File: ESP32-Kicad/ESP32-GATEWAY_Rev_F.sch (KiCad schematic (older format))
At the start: 90 parts, among them CON1 NA(NH1x20), Q3 Q12MHz/20pF/30ppm/2P/HC-49SM(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, Q4 BC817-40(SOT23), Q5 BC817-40(SOT23), T1 DTC114YKA, U2 SY8089AAAC(SOT23-5), U3 ESP32-WROOM-32D-4MB, U4 LAN8710A-EZC(QFN32), U5 CH340T(SSOP20W)

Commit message: Proyecto de kicad actualizado.
 Se eliminó completamente la sección de la MicroSD
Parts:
- removed BUT1: T1107A(6x3,8x2,5MM), OLIMEX_Buttons-FP:T1107A(6x3,8x2,5MM), symbol ESP32-GATEWAY_Rev_F:SIDE_WTCM-TR(3x4)
- removed C10: 47uF/6.3V/20%/X5R/C0805, OLIMEX_RLC-FP:C_0805_5MIL_DWS, symbol ESP32-GATEWAY_Rev_F:C
- removed L4: FB0805/600R/2A, OLIMEX_RLC-FP:L_0805_5MIL_DWS, symbol ESP32-GATEWAY_Rev_F:L
- removed MICRO_SD1: TFC-WXCP11-08-LF, OLIMEX_Connectors-FP:TFC-WXCP11-08-LF, symbol ESP32-GATEWAY_Rev_F:MICRO_SD(TFC-WXCP11-08-LF)
- removed R10, R11, R9: NA/R0603, OLIMEX_RLC-FP:R_0603_5MIL_DWS, symbol ESP32-GATEWAY_Rev_F:R
- removed R16: 220R/R0603, OLIMEX_RLC-FP:R_0603_5MIL_DWS, symbol ESP32-GATEWAY_Rev_F:R
- removed R2, R7, R8: 2.2k/R0603, OLIMEX_RLC-FP:R_0603_5MIL_DWS, symbol ESP32-GATEWAY_Rev_F:R
- removed R43: 10R/R0603, OLIMEX_RLC-FP:R_0603_5MIL_DWS, symbol ESP32-GATEWAY_Rev_F:R
- removed R45: 10k/R0603, OLIMEX_RLC-FP:R_0603_5MIL_DWS, symbol ESP32-GATEWAY_Rev_F:R
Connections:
- net labels added: GPI34
- net labels removed: GPI34\BUT1
- wire segments 428 -> 383
- no-connect marks 19 -> 31
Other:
- note added: "Debil pull-down interno. Requiere de LOW para descargar codigo. Dejar desconectado o a masa. Listo"
- note added: "Dejar la pull-up para habilitar los logs\ndurante el boot. Listo"
- note added: "Incluido en el bootstrap pero no se usa. Dejado por las dudas."
- note added: "Requiere de LOW para descargar codigo\nDejar desconectado o a masa. Listo."
- note added: "Se necesita LOW o desconectado para la flash con 3v3. Listo"
- note added: "Usar. Listo"
- note removed: "Arranca con PWM. \nTestear con ds18b20"
- note removed: "Debil pull-down interno. Requiere de LOW para descargar codigo. Dejar desconectado o a masa."
- note removed: "Debil pull-down interno. Requiere de LOW para descargar codigo. Dejar desconectado o a masa. Faltaria un pulldown."
- note removed: "Dejar la pull-up para habilitar los logs\ndurante el boot. Evitar usar\n\n"
- note removed: "Incluido en el bootstrap pero no se usa. Se puede usar tranquilamente."
- note removed: "Incluido en ll bootstrap pero no se usa.\nSe puede usar tranquilamente."
- note removed: "No Usar. Listo"
- note removed: "No está\n"
- note removed: "No usar. Se necesita LOW o desconectado para la flash con 3v3."
- note removed: "No usar. Se necesita LOW o desconectado\n para la flash con 3v3.\n\n"
- note removed: "Probado con ds18b20 y pullup interno."
- note removed: "Probado con ds18b20 y pullup interno.\n"
- note removed: "Requiere de LOW para descargar codigo\nDejar desconectado o a masa."
- note removed: "SD/MMC Card"
- note removed: "Se necesita LOW o desconectado para la flash con 3v3."
- note removed: "Se puede usar con duda."
- note removed: "Solo entrada. Sin pulldown-pullup"
- moved on the sheet: R29, R3

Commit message: Proyecto de kicad actualizado
Se retiró la parte del programador USB y otras menores asociadas a esta.
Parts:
- removed C21, C22: 27pF/50V/5%/C0G/C0603, OLIMEX_RLC-FP:C_0603_5MIL_DWS, symbol ESP32-GATEWAY_Rev_F:C
- removed C23: 22uF/6.3V/20%/X5R/C0603, OLIMEX_RLC-FP:C_0603_5MIL_DWS, symbol ESP32-GATEWAY_Rev_F:C
- removed C24: 100nF/50V/20%/Y5V/C0603, OLIMEX_RLC-FP:C_0603_5MIL_DWS, symbol ESP32-GATEWAY_Rev_F:C
- removed D1, D3: 1N5819S4/SOD123, OLIMEX_Diodes-FP:SOD-123_1C-2A_KA, symbol ESP32-GATEWAY_Rev_F:D_Schottky
- removed D4: BAT54C(SOT23-3), OLIMEX_Diodes-FP:SOT23-3, symbol ESP32-GATEWAY_Rev_F:BAT54C(SOT23-3)
- removed Q3: Q12MHz/20pF/30ppm/2P/HC-49SM(SMD), OLIMEX_Crystal-FP:Q_49U3HMS, symbol ESP32-GATEWAY_Rev_F:Crystal
- removed Q4, Q5: BC817-40(SOT23), OLIMEX_Transistors-FP:SOT23, symbol ESP32-GATEWAY_Rev_F:Q_NPN_BEC
- removed R35, R40: 10k/R0603, OLIMEX_RLC-FP:R_0603_5MIL_DWS, symbol ESP32-GATEWAY_Rev_F:R
- removed R37: 220R/R0603, OLIMEX_RLC-FP:R_0603_5MIL_DWS, symbol ESP32-GATEWAY_Rev_F:R
- removed R41, R42: 1k/R0603, OLIMEX_RLC-FP:R_0603_5MIL_DWS, symbol ESP32-GATEWAY_Rev_F:R
- removed U5: CH340T(SSOP20W), OLIMEX_IC-FP:SSOP-20W, symbol ESP32-GATEWAY_Rev_F:CH340T(SSOP20W)
- added J10: Conn_01x02_Male, Connector_PinHeader_2.54mm:PinHeader_1x02_P2.54mm_Vertical, symbol Connector:Conn_01x02_Male
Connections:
- net labels removed: D_Com
- wire segments 383 -> 324
- no-connect marks 31 -> 27
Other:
- note removed: "Auto program\n"
- note removed: "DTR RTS->EN IO0"
- note removed: "Debil pull-down interno.\nRequiere de LOW para descargar codigo\nDejar desconectado o a masa."

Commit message: Proyecto de Kicad actualizado
Fuente corregida. Programador agregado. Cambios menores.
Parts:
- removed CON1: NA(NH1x20), OLIMEX_Connectors-FP:HN1x20, symbol ESP32-GATEWAY_Rev_F:CON20
- removed D2: SMBJ6.0A(DO-214AA), OLIMEX_Diodes-FP:DO214AA_1(K)-2(A), symbol ESP32-GATEWAY_Rev_F:SMBJ6.0A
- removed D6: 1N5822/SS34/SMA, OLIMEX_Diodes-FP:SMA-KA, symbol ESP32-GATEWAY_Rev_F:D_Schottky
- removed FET2: WPM2015-3/TR, OLIMEX_Transistors-FP:SOT23, symbol ESP32-GATEWAY_Rev_F:P-MOS+DIOD
- removed J10: Conn_01x02_Male, Connector_PinHeader_2.54mm:PinHeader_1x02_P2.54mm_Vertical, symbol Connector:Conn_01x02_Male
- removed LED_E1: Closed, OLIMEX_Jumpers-FP:SJ, symbol ESP32-GATEWAY_Rev_F:SJ
- removed PWRLED1: LED/RED/0603, OLIMEX_LEDs-FP:LED_0603_KA, symbol ESP32-GATEWAY_Rev_F:LED
- removed R30: 1M/R0603, OLIMEX_RLC-FP:R_0603_5MIL_DWS, symbol ESP32-GATEWAY_Rev_F:R
- removed R4: 2.2k/R0603, OLIMEX_RLC-FP:R_0603_5MIL_DWS, symbol ESP32-GATEWAY_Rev_F:R
- removed RST1: T1107A(6x3,8x2,5MM), OLIMEX_Buttons-FP:T1107A(6x3,8x2,5MM), symbol ESP32-GATEWAY_Rev_F:SIDE_WTCM-TR(3x4)
- added CON1: Conn_01x13_Male, Connector_PinHeader_2.54mm:PinHeader_1x13_P2.54mm_Vertical, symbol Connector:Conn_01x13_Male
- added J1: Conn_01x07_Male, Connector_PinHeader_2.54mm:PinHeader_1x07_P2.54mm_Horizontal, symbol Connector:Conn_01x07_Male
- C1: value 47uF/6.3V/20%/X5R/C0805 -> 10uF/6.3V/20%/X5R/C0805/1mΩ
- C3, C4: value 47uF/6.3V/20%/X5R/C0805 -> 4.7uF/6.3V/20%/X5R/C0805/1mΩ
- L2: value 2.2uH/1.5A/DCR=72mR/20%/3.00x3.00x1.50mm/CD32(NR3015T2R2M) -> 2.2uH/1.5A/DCR=35mR/20%/3.00x3.00x1.50mm/CD32(NR3015T2R2M)
- R19: value 220k/R0603 -> 442k/1%/50mW/R0603
- R20: value 49.9k/1%/R0603 -> 100k/1%/63mw/R0603
- R54: value NA/R0603 -> 10K/R0603
- U2: value SY8089AAAC(SOT23-5) -> TLV62569DBVT(SOT23-5)
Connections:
- net labels removed: +5V_EXT, +5V_USB
- wire segments 324 -> 293
- no-connect marks 27 -> 26
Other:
- note added: "(logs)\n"
- note added: "Dejado por las dudas."
- note added: "Dejado por las dudas.\n"
- note added: "ESP-WROOM-32\n MODULO"
- note added: "Fiduciales"
- note added: "Fuente de Alimentación"
- note added: "Programador"
- note removed: "+5V_Only!!!"
- note removed: "Arranca con PWM. Probado con ds18b20 y pullup interno.\n"
- note removed: "Arranca con PWM. Testear con ds18b20"
- note removed: "Buttons"
- note removed: "Debil pull-down interno. Requiere de LOW para descargar codigo. Dejar desconectado o a masa. Listo"
- note removed: "Debil pull-up interno. \nCon 1 entra a boot normal\nCon 0, descarga codigo."
- note removed: "Dejar la pull-up para habilitar los logs durante el boot. Evitar usar\n"
- note removed: "Dejar la pull-up para habilitar los logs\ndurante el boot. Listo"
- note removed: "ESP-WROOM-32\n MODULE"
- note removed: "Fiducials"
- note removed: "Incluido en el bootstrap pero no se usa. Dejado por las dudas."
- note removed: "NO usar. Lo necesita la parte de Ethernet"
- note removed: "NO usar. Lo necesita la parte de Ethernet. Listo"
- note removed: "Power Supply"
- note removed: "Requiere de LOW para descargar codigo\nDejar desconectado o a masa. Listo."
- note removed: "Se necesita LOW o desconectado para la flash con 3v3. Listo"
- note removed: "Se puede usar."
- note removed: "Se usa para habilitar el esp32. Dejar un pin para el programador externo"
- note removed: "TX/RX para programarlo\n"
- note removed: "USB to UART"
- moved on the sheet: C1, C3, C4, FID1, FID2, FID3, GND1, L2, MH1, MH2, R19, R20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

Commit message: Proyecto de kicad actualizado.
Se agregaron los conectores adecuados y se rutearon los gpio para estos. Queda pendiente ubicarlos correctamente para evitar el solapamiento de estos. Se acomodaron algunas resistencias y se eliminaron pistas viejas innecesarias.
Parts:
- removed CON1: Conn_01x13_Male, Connector_PinHeader_2.54mm:PinHeader_1x13_P2.54mm_Vertical, symbol Connector:Conn_01x13_Male
- removed USB-UART1: MISB-SWMM-5B-LF(USB_MICRO), OLIMEX_Connectors-FP:USB-MICRO_MISB-SWMM-5B_LF, symbol ESP32-GATEWAY_Rev_F:USB-MINI
- added PUERTA1, PUERTA2: Conn_01x02_Female, Connector_Molex:Molex_KK-254_AE-6410-02A_1x02_P2.54mm_Vertical, symbol Connector:Conn_01x02_Female
- added TEMP1, TEMP2: Conn_01x03_Female, Connector_Molex:Molex_KK-254_AE-6410-03A_1x03_P2.54mm_Vertical, symbol Connector:Conn_01x03_Female
- added USB-UART2: USB_B_Micro, Connector_USB:USB_Micro-B_Amphenol_10104110_Horizontal, symbol Connector:USB_B_Micro
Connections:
- net labels added: GPIO13\TEMP1, GPIO14\TEMP2, GPIO32\PUERTA1, GPIO33\PUERTA2
- net labels removed: GPIO13\HS2_DATA3, GPIO14\HS2_CLK, GPIO32, GPIO33\LED
- wire segments 293 -> 281
- no-connect marks 26 -> 20
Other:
- note added: "Sensores"
- note removed: "Dejado por las dudas.\n"
- note removed: "Extension"
- note removed: "Usar. Listo"
- note removed: "Usar. Listo\n"

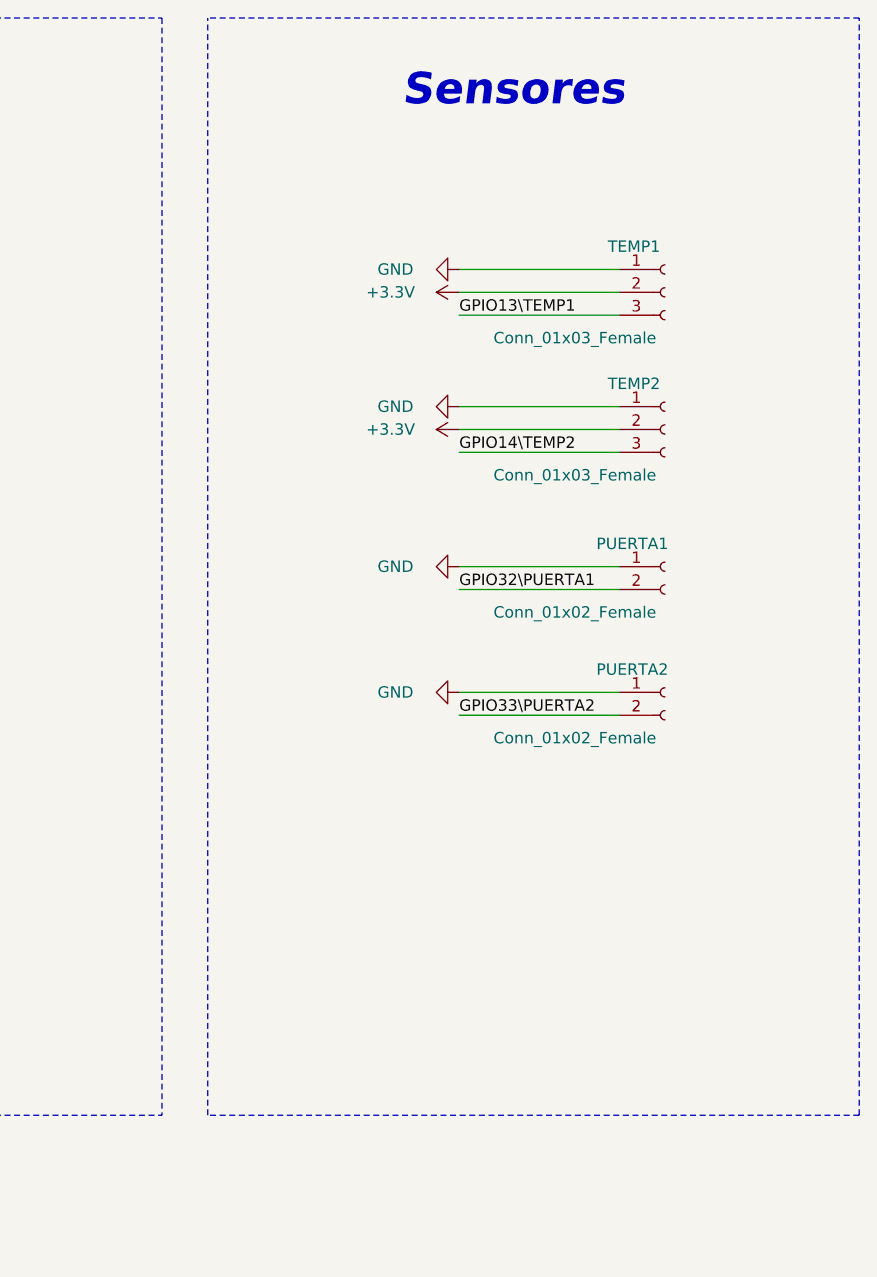
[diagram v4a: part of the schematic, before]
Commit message: Proyecto en kicad actualizado
Se modificó la posición de la pinera para programar la placa. Recolocaron los conectores de los sensores y se agregaron sus resistencias mas el modelo 3D de todo esto.
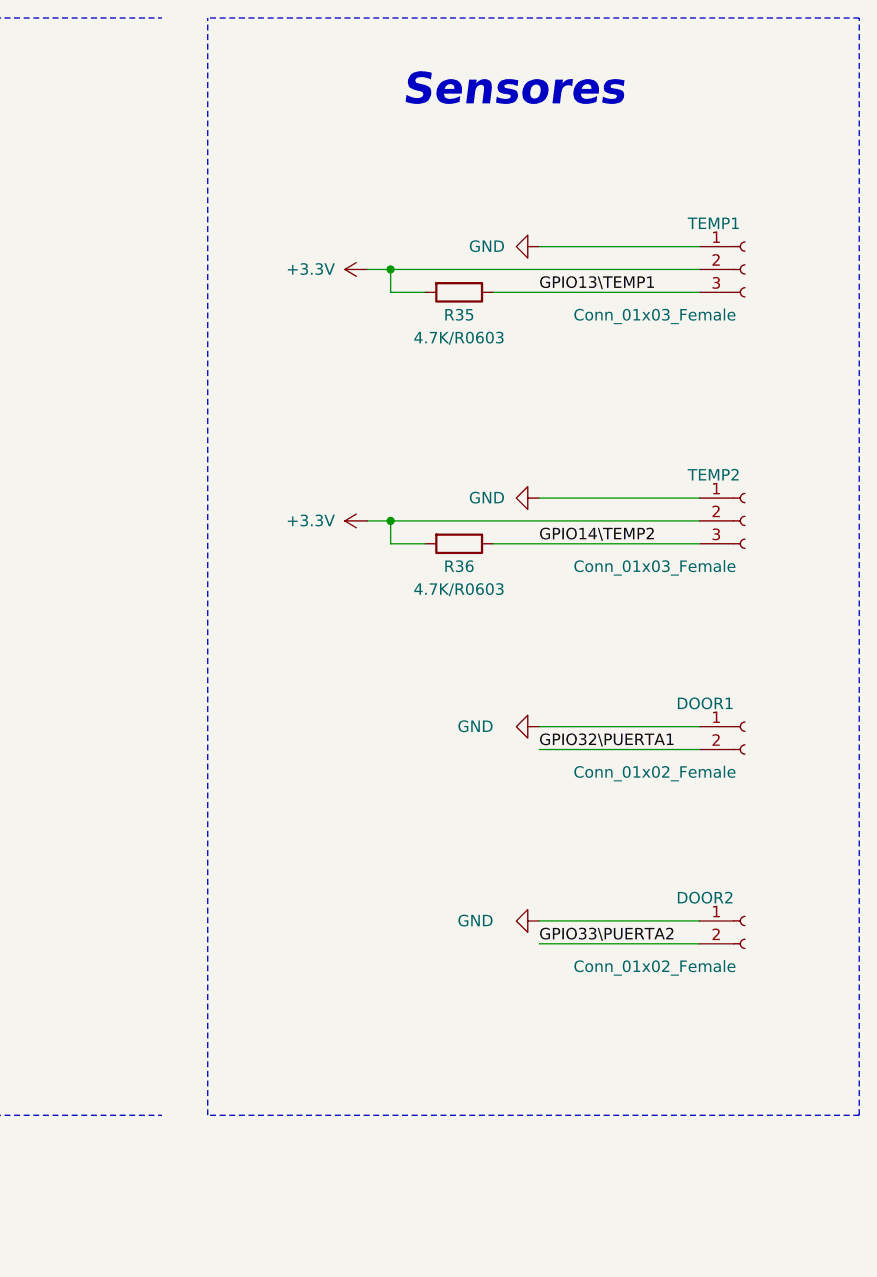
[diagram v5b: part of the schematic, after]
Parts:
- added R35, R36: 4.7K/R0603, Resistor_SMD:R_0603_1608Metric_Pad0.98x0.95mm_HandSolder, symbol Device:R
- J1: footprint Connector_PinHeader_2.54mm:PinHeader_1x07_P2.54mm_Horizontal -> Connector_PinHeader_2.54mm:PinHeader_1x07_P2.54mm_Vertical
- renumbered PUERTA1 to DOOR1, PUERTA2 to DOOR2
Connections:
- wire segments 281 -> 287
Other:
- moved on the sheet: DOOR1, DOOR2, TEMP1, TEMP2
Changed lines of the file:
@@
 F 0 "J1" H 15222 6874 50  0000 R CNN
 F 1 "Conn_01x07_Male" H 15222 6783 50  0000 R CNN
-F 2 "Connector_PinHeader_2.54mm:PinHeader_1x07_P2.54mm_Horizontal" H 15250 6850 50  0001 C CNN
+F 2 "Connector_PinHeader_2.54mm:PinHeader_1x07_P2.54mm_Vertical" H 15250 6850 50  0001 C CNN
 F 3 "~" H 15250 6850 50  0001 C CNN
 	1    15250 6850
@@
 	15050 6850 13750 6850
 Wire Notes Line
-	19550 700  19550 5500
-Wire Notes Line
 	19750 5500 19750 700
 Text Label 13750 6950 0    50   ~ 0
@@
 NoConn ~ 2000 2650
 $Comp
-L Connector:Conn_01x02_Female PUERTA1
+L Connector:Conn_01x02_Female DOOR1
 U 1 1 61288657
-P 21750 3100
-F 0 "PUERTA1" H 21450 3200 50  0000 L CNN
-F 1 "Conn_01x02_Female" H 21000 2900 50  0000 L CNN
-F 2 "Connector_Molex:Molex_KK-254_AE-6410-02A_1x02_P2.54mm_Vertical" H 21750 3100 50  0001 C CNN
-F 3 "~" H 21750 3100 50  0001 C CNN
-	1    21750 3100
-	1    0    0    -1
-$EndComp
-$Comp
-L Connector:Conn_01x02_Female PUERTA2
+P 22100 3800
+F 0 "DOOR1" H 21800 3900 50  0000 L CNN
+F 1 "Conn_01x02_Female" H 21350 3600 50  0000 L CNN
+F 2 "Connector_Molex:Molex_KK-254_AE-6410-02A_1x02_P2.54mm_Vertical" H 22100 3800 50  0001 C CNN
+F 3 "~" H 22100 3800 50  0001 C CNN
+	1    22100 3800
+	1    0    0    -1
+$EndComp
+$Comp
+L Connector:Conn_01x02_Female DOOR2
 U 1 1 6128A81D
-P 21750 3650
-F 0 "PUERTA2" H 21450 3750 50  0000 L CNN
-F 1 "Conn_01x02_Female" H 21000 3450 50  0000 L CNN
-F 2 "Connector_Molex:Molex_KK-254_AE-6410-02A_1x02_P2.54mm_Vertical" H 21750 3650 50  0001 C CNN
-F 3 "~" H 21750 3650 50  0001 C CNN
-	1    21750 3650
+P 22100 4650
+F 0 "DOOR2" H 21800 4750 50  0000 L CNN
+F 1 "Conn_01x02_Female" H 21350 4450 50  0000 L CNN
+F 2 "Connector_Molex:Molex_KK-254_AE-6410-02A_1x02_P2.54mm_Vertical" H 22100 4650 50  0001 C CNN
+F 3 "~" H 22100 4650 50  0001 C CNN
+	1    22100 4650
 	1    0    0    -1
 $EndComp
@@
 L ESP32-GATEWAY_Rev_F:GND #PWR0102
 U 1 1 6128BF60
-P 20850 3650
-F 0 "#PWR0102" H 20850 3400 50  0001 C CNN
-F 1 "GND" V 20850 3450 50  0000 R CNN
-F 2 "" H 20850 3650 60  0000 C CNN
-F 3 "" H 20850 3650 60  0000 C CNN
-	1    20850 3650
+P 21200 4650
+F 0 "#PWR0102" H 21200 4400 50  0001 C CNN
+F 1 "GND" V 21200 4450 50  0000 R CNN
+F 2 "" H 21200 4650 60  0000 C CNN
+F 3 "" H 21200 4650 60  0000 C CNN
+	1    21200 4650
 	0    1    1    0
 $EndComp
@@
 L ESP32-GATEWAY_Rev_F:GND #PWR0103
 U 1 1 612A5050
-P 20850 3100
-F 0 "#PWR0103" H 20850 2850 50  0001 C CNN
-F 1 "GND" V 20850 2900 50  0000 R CNN
-F 2 "" H 20850 3100 60  0000 C CNN
-F 3 "" H 20850 3100 60  0000 C CNN
-	1    20850 3100
-	0    1    1    0
-$EndComp
-Text Label 20850 3750 0    50   ~ 0
+P 21200 3800
+F 0 "#PWR0103" H 21200 3550 50  0001 C CNN
+F 1 "GND" V 21200 3600 50  0000 R CNN
+F 2 "" H 21200 3800 60  0000 C CNN
+F 3 "" H 21200 3800 60  0000 C CNN
+	1    21200 3800
+	0    1    1    0
+$EndComp
+Text Label 21200 4750 0    50   ~ 0
 GPIO33\PUERTA2
 $Comp
 L Connector:Conn_01x03_Female TEMP1
 U 1 1 614AF2AC
-P 21750 1900
-F 0 "TEMP1" H 21500 2100 50  0000 L CNN
-F 1 "Conn_01x03_Female" H 21000 1700 50  0000 L CNN
-F 2 "Connector_Molex:Molex_KK-254_AE-6410-03A_1x03_P2.54mm_Vertical" H 21750 1900 50  0001 C CNN
-F 3 "~" H 21750 1900 50  0001 C CNN
-	1    21750 1900
+P 22100 1800
+F 0 "TEMP1" H 21850 2000 50  0000 L CNN
+F 1 "Conn_01x03_Female" H 21350 1600 50  0000 L CNN
+F 2 "Connector_Molex:Molex_KK-254_AE-6410-03A_1x03_P2.54mm_Vertical" H 22100 1800 50  0001 C CNN
+F 3 "~" H 22100 1800 50  0001 C CNN
+	1    22100 1800
 	1    0    0    -1
 $EndComp
@@
 L Connector:Conn_01x03_Female TEMP2
 U 1 1 614B142C
-P 21750 2500
-F 0 "TEMP2" H 21500 2700 50  0000 L CNN
-F 1 "Conn_01x03_Female" H 21000 2300 50  0000 L CNN
-F 2 "Connector_Molex:Molex_KK-254_AE-6410-03A_1x03_P2.54mm_Vertical" H 21750 2500 50  0001 C CNN
-F 3 "~" H 21750 2500 50  0001 C CNN
-	1    21750 2500
+P 22100 2900
+F 0 "TEMP2" H 21850 3100 50  0000 L CNN
+F 1 "Conn_01x03_Female" H 21350 2700 50  0000 L CNN
+F 2 "Connector_Molex:Molex_KK-254_AE-6410-03A_1x03_P2.54mm_Vertical" H 22100 2900 50  0001 C CNN
+F 3 "~" H 22100 2900 50  0001 C CNN
+	1    22100 2900
 	1    0    0    -1
 $EndComp
@@
 L ESP32-GATEWAY_Rev_F:+3.3V #PWR0104
 U 1 1 614B2E1D
-P 20850 1900
-F 0 "#PWR0104" H 20850 1750 50  0001 C CNN
-F 1 "+3.3V" V 20850 2200 50  0000 C CNN
-F 2 "" H 20850 1900 60  0000 C CNN
-F 3 "" H 20850 1900 60  0000 C CNN
-	1    20850 1900
+P 20450 1800
+F 0 "#PWR0104" H 20450 1650 50  0001 C CNN
+F 1 "+3.3V" V 20450 2050 50  0000 C CNN
+F 2 "" H 20450 1800 60  0000 C CNN
+F 3 "" H 20450 1800 60  0000 C CNN
+	1    20450 1800
 	0    -1   -1   0
 $EndComp
@@
 L ESP32-GATEWAY_Rev_F:+3.3V #PWR0105
 U 1 1 614CCBB7
-P 20850 2500
-F 0 "#PWR0105" H 20850 2350 50  0001 C CNN
-F 1 "+3.3V" V 20850 2800 50  0000 C CNN
-F 2 "" H 20850 2500 60  0000 C CNN
-F 3 "" H 20850 2500 60  0000 C CNN
-	1    20850 2500
+P 20450 2900
+F 0 "#PWR0105" H 20450 2750 50  0001 C CNN
+F 1 "+3.3V" V 20450 3150 50  0000 C CNN
+F 2 "" H 20450 2900 60  0000 C CNN
+F 3 "" H 20450 2900 60  0000 C CNN
+	1    20450 2900
 	0    -1   -1   0
 $EndComp
-Text Label 20850 3200 0    50   ~ 0
+Text Label 21200 3900 0    50   ~ 0
 GPIO32\PUERTA1
 $Comp
 L ESP32-GATEWAY_Rev_F:GND #PWR0106
 U 1 1 61687BE2
-P 20850 2400
-F 0 "#PWR0106" H 20850 2150 50  0001 C CNN
-F 1 "GND" V 20850 2200 50  0000 R CNN
-F 2 "" H 20850 2400 60  0000 C CNN
-F 3 "" H 20850 2400 60  0000 C CNN
-	1    20850 2400
+P 21200 2800
+F 0 "#PWR0106" H 21200 2550 50  0001 C CNN
+F 1 "GND" V 21200 2650 50  0000 R CNN
+F 2 "" H 21200 2800 60  0000 C CNN
+F 3 "" H 21200 2800 60  0000 C CNN
+	1    21200 2800
 	0    1    1    0
 $EndComp
@@
 L ESP32-GATEWAY_Rev_F:GND #PWR0107
 U 1 1 616A2220
-P 20850 1800
-F 0 "#PWR0107" H 20850 1550 50  0001 C CNN
-F 1 "GND" V 20850 1600 50  0000 R CNN
-F 2 "" H 20850 1800 60  0000 C CNN
-F 3 "" H 20850 1800 60  0000 C CNN
-	1    20850 1800
-	0    1    1    0
-$EndComp
-Text Label 20850 2000 0    50   ~ 0
+P 21200 1700
+F 0 "#PWR0107" H 21200 1450 50  0001 C CNN
+F 1 "GND" V 21200 1550 50  0000 R CNN
+F 2 "" H 21200 1700 60  0000 C CNN
+F 3 "" H 21200 1700 60  0000 C CNN
+	1    21200 1700
+	0    1    1    0
+$EndComp
+Text Label 21200 1900 0    50   ~ 0
 GPIO13\TEMP1
-Text Label 20850 2600 0    50   ~ 0
+Text Label 21200 3000 0    50   ~ 0
 GPIO14\TEMP2
 Wire Wire Line
-	20850 2400 21550 2400
-Wire Wire Line
-	20850 2500 21550 2500
-Wire Wire Line
-	20850 2600 21550 2600
-Wire Wire Line
-	20850 1800 21550 1800
-Wire Wire Line
-	20850 1900 21550 1900
-Wire Wire Line
-	20850 2000 21550 2000
-Wire Wire Line
-	20850 3100 21550 3100
-Wire Wire Line
-	20850 3200 21550 3200
-Wire Wire Line
-	20850 3650 21550 3650
-Wire Wire Line
-	20850 3750 21550 3750
+	21200 2800 21900 2800
+Wire Wire Line
+	21200 1700 21900 1700
+Wire Wire Line
+	21200 3800 21900 3800
+Wire Wire Line
+	21200 3900 21900 3900
+Wire Wire Line
+	21200 4650 21900 4650
+Wire Wire Line
+	21200 4750 21900 4750
 NoConn ~ 16700 3500
+$Comp
+L Device:R R35
+U 1 1 614AF891
+P 20850 1900
+F 0 "R35" V 20950 1900 50  0000 C CNN
+F 1 "4.7K/R0603" V 21050 1900 50  0000 C CNN
+F 2 "Resistor_SMD:R_0603_1608Metric_Pad0.98x0.95mm_HandSolder" V 20780 1900 50  0001 C CNN
+F 3 "~" H 20850 1900 50  0001 C CNN
+	1    20850 1900
+	0    1    1    0
+$EndComp
+Wire Wire Line
+	21000 1900 21900 1900
+Wire Wire Line
+	20450 1800 20550 1800
+Wire Wire Line
+	20550 1800 20550 1900
+Wire Wire Line
+	20550 1900 20700 1900
+Wire Wire Line
+	20550 1800 21900 1800
+Connection ~ 20550 1800
+$Comp
+L Device:R R36
+U 1 1 61518737
+P 20850 3000
+F 0 "R36" V 20950 3000 50  0000 C CNN
+F 1 "4.7K/R0603" V 21050 3000 50  0000 C CNN
+F 2 "Resistor_SMD:R_0603_1608Metric_Pad0.98x0.95mm_HandSolder" V 20780 3000 50  0001 C CNN
+F 3 "~" H 20850 3000 50  0001 C CNN
+	1    20850 3000
+	0    1    1    0
+$EndComp
+Wire Wire Line
+	21000 3000 21900 3000
+Wire Wire Line
+	20550 2900 20550 3000
+Wire Wire Line
+	20550 3000 20700 3000
+Wire Wire Line
+	20450 2900 20550 2900
+Connection ~ 20550 2900
+Wire Wire Line
+	20550 2900 21900 2900
 $EndSCHEMATC
